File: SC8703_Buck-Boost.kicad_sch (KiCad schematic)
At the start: 0 parts

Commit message: 补充中文版数据手册，原理图放置SC8703芯片
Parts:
- added U1: SC8703, Package_DFN_QFN:QFN-32-1EP_4x4mm_P0.4mm_EP2.65x2.65mm, symbol Zeruns:SC8703
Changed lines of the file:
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@@
 	(generator_version "9.0")
 	(paper "A4")
+	(symbol
+		(lib_id "Zeruns:SC8703")
+		(at 149.86 91.44 0)
+		(unit 1)
+		(exclude_from_sim no)
+		(in_bom yes)
+		(on_board yes)
+		(dnp no)
+		(fields_autoplaced yes)
+		(property "Reference" "U1"
+			(at 149.86 63.5 0)
+			(effects
+				(font
+					(size 1.27 1.27)
+				)
+			)
+		)
+		(property "Value" "SC8703"
+			(at 149.86 66.04 0)
+			(effects
+				(font
+					(size 1.27 1.27)
+				)
+			)
+		)
+		(property "Footprint" "Package_DFN_QFN:QFN-32-1EP_4x4mm_P0.4mm_EP2.65x2.65mm"
+			(at 150.114 121.92 0)
+			(effects
+				(font
+					(size 1.27 1.27)
+				)
+				(hide yes)
+			)
+		)
+		(property "Datasheet" "kicad-embed://SouthChip-Regular_SC8703_datasheet_20241224.pdf"
+			(at 149.86 124.206 0)
+			(effects
+				(font
+					(size 1.27 1.27)
+				)
+				(hide yes)
+			)
+		)
+		(property "Description" "南芯半导体（SouthChip）SC8703 高效率同步 4 管升降压控制器，支持 2.7V~36V 超宽输入输出电压范围，集成 10V/2A 栅极驱动器，可在输入电压高于、低于或等于输出电压时稳定输出，适用于 USB PD、车充、工业设备等场景。"
+			(at 150.368 127 0)
+			(effects
+				(font
+					(size 1.27 1.27)
+				)
+				(hide yes)
+			)
+		)
+		(pin "2"
+		)
+		(pin "1"
+		)
+		(pin "15"
+		)
+		(pin "4"
+		)
+		(pin "31"
+		)
+		(pin "5"
+		)
+		(pin "10"
+		)
+		(pin "33"
+		)
+		(pin "3"
+		)
+		(pin "6"
+		)
+		(pin "7"
+		)
+		(pin "8"
+		)
+		(pin "9"
+		)
+		(pin "12"
+		)
+		(pin "11"
+		)
+		(pin "13"
+		)
+		(pin "14"
+		)
+		(pin "16"
+		)
+		(pin "32"
+		)
+		(pin "30"
+		)
+		(pin "28"
+		)
+		(pin "27"
+		)
+		(pin "26"
+		)
+		(pin "25"
+		)
+		(pin "29"
+		)
+		(pin "22"
+		)
+		(pin "18"
+		)
+		(pin "24"
+		)
+		(pin "20"
+		)
+		(pin "17"
+		)
+		(pin "21"
+		)
+		(pin "23"
+		)
+		(pin "19"
+		)
+		(instances
+			(project ""
+				(path "/00808dcd-76cb-4382-86f8-b718334c603a"
+					(reference "U1")
+					(unit 1)
+				)
+			)
+		)
+	)
 	(sheet_instances
 		(path "/"

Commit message: 原理图完成5%
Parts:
- added C1, C2: 10nF, Capacitor_SMD:C_0402_1005Metric_Pad0.74x0.62mm_HandSolder, symbol Device:C
- added J1: XT30PW-M, Connector_AMASS:AMASS_XT30PW-M_1x02_P2.50mm_Horizontal, symbol Connector:Conn_01x02_Socket
- added J2: Conn_01x02_Socket, Connector_AMASS:AMASS_XT30PW-F_1x02_P2.50mm_Horizontal, symbol Connector:Conn_01x02_Socket
- added Q1, Q2, Q3, Q4: XRS100N06LD, Zeruns:DFN-8_L3.0-W3.0-P0.65-BL-4, symbol Simulation_SPICE:NMOS
- added R1, R3: 12.1k, Resistor_SMD:R_0402_1005Metric_Pad0.72x0.64mm_HandSolder, symbol Device:R
- added R2, R4: 5mR, Resistor_SMD:R_1206_3216Metric_Pad1.30x1.75mm_HandSolder, symbol Device:R
- added RV2: 200k, Potentiometer_THT:Potentiometer_Bourns_3296W_Vertical, symbol Device:R_Potentiometer
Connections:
- net at U1.11 (ILIM1): now also C1.2, R1.2
- net at U1.12 (ILIM2): now also C2.2, R3.2
- new net: Q1.3 (S), Q2.1 (D)
- new net: Q1.1 (D), R2.2
- new net: J1.2 (Pin_2), R2.1
- new net: R3.1, RV2.1, RV2.2
- new net: Q3.1 (D), R4.1
- new net: Q3.3 (S), Q4.1 (D)
- new net GND: C1.1, C2.1, R1.1, RV2.3
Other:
- moved on the sheet: U1

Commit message: 原理图完成80%，上传数据手册
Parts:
- added C10, C11, C5, C6, C7, C9: 10uF, Capacitor_SMD:C_1206_3216Metric_Pad1.33x1.80mm_HandSolder, symbol Device:C
- added C12, C17, C18, C8: 100nF, Capacitor_SMD:C_0402_1005Metric_Pad0.74x0.62mm_HandSolder, symbol Device:C
- added C13: 15nF, Capacitor_SMD:C_0402_1005Metric_Pad0.74x0.62mm_HandSolder, symbol Device:C
- added C14, C15: 47pF, Capacitor_SMD:C_0402_1005Metric_Pad0.74x0.62mm_HandSolder, symbol Device:C
- added C16, C19, C20: 1uF, Capacitor_SMD:C_0402_1005Metric_Pad0.74x0.62mm_HandSolder, symbol Device:C
- added C21, C22: NC, Capacitor_SMD:C_0603_1608Metric_Pad1.08x0.95mm_HandSolder, symbol Device:C
- added C3: 220uF, Capacitor_SMD:CP_Elec_10x10.5, symbol Device:C_Polarized_US
- added C4: 330uF, Capacitor_SMD:CP_Elec_10x10.5, symbol Device:C_Polarized_US
- added D1, D2: TPB2A100-123FL, Diode_SMD:D_SOD-123F, symbol Device:D_Schottky
- added J3: USB_C_Receptacle_USB2.0_16P, Connector_USB:USB_C_Receptacle_HCTL_HC-TYPE-C-16P-01A, symbol Connector:USB_C_Receptacle_USB2.0_16P
- added L1: 4.7uH, Inductor_SMD:L_APV_APH1265, symbol Device:L
- added R10, R11, R12, R9: 510R, Resistor_SMD:R_0402_1005Metric_Pad0.72x0.64mm_HandSolder, symbol Device:R
- added R13, R14, R15, R16: 0R, Resistor_SMD:R_0603_1608Metric_Pad0.98x0.95mm_HandSolder, symbol Device:R
- added R17, R18: NC, Resistor_SMD:R_0603_1608Metric_Pad0.98x0.95mm_HandSolder, symbol Device:R
- added R5: NC, Resistor_SMD:R_0402_1005Metric_Pad0.72x0.64mm_HandSolder, symbol Device:R
- added R6: 68k, Resistor_SMD:R_0402_1005Metric_Pad0.72x0.64mm_HandSolder, symbol Device:R
- added R7: 15k, Resistor_SMD:R_0402_1005Metric_Pad0.72x0.64mm_HandSolder, symbol Device:R
- added R8: 1.74k, Resistor_SMD:R_0402_1005Metric_Pad0.72x0.64mm_HandSolder, symbol Device:R
- added RV1: 50k, Potentiometer_THT:Potentiometer_Bourns_3296X_Horizontal, symbol Device:R_Potentiometer
- added U2: CH224Q, Zeruns:DFN-10_L2.0-W2.0-P0.40-BL-EP, symbol Zeruns:CH224Q
- J2: value Conn_01x02_Socket -> XT30PW-F
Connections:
- net GND: now also J1.1 (Pin_1), J2.1 (Pin_1), Q2.3 (S), Q4.3 (S), U1.1 (CE#), U1.14 (AGND), U1.2 (AGND), U1.25 (PGND), U1.33 (PGND), U1.9 (AGND), C10.2, C11.2, C12.1, C13.1, C16.2, C19.2, C20.2, C21.1, C22.1, C3.2, C4.2, C5.2, C6.2, C7.2, C8.1, C9.2, R5.1, R6.1, R8.1
- net SW1: now reaches Q1.3 (S), Q2.1 (D)
- net SW1: now also U1.27 (SW1), C17.2, L1.1, R17.2
- net at Q2.2 (G): now also R14.2
- net ILIM1: now reaches C1.2, R1.2, U1.11 (ILIM1)
- net at Q1.1 (D), R2.2: now also R10.1
- net at Q1.2 (G): now also R13.2
- net VOUT: now reaches J2.2 (Pin_2)
- net VOUT: now also R4.2, U1.19 (VOUT), C10.1, C11.1, C12.2, C20.1, C4.1, C9.1, R12.1, RV1.3
- net VIN: now reaches J1.2 (Pin_2), R2.1
- net VIN: now also U1.30 (VIN), U1.7 (UVLO), C16.1, C3.1, C5.1, C6.1, C7.1, C8.2, R9.1
- net ILIM2: now reaches C2.2, R3.2, U1.12 (ILIM2)
- net at Q3.1 (D), R4.1: now also R11.1
- net at Q3.2 (G): now also R15.1
- net SW2: now reaches Q3.3 (S), Q4.1 (D)
- net SW2: now also U1.22 (SW2), C18.2, L1.2, R18.2
- net FREQ: now reaches U1.10 (FREQ)
- net FREQ: now also R5.2
- net at U1.15 (COMP): now also R7.2
- net FB: now reaches U1.16 (FB)
- net FB: now also R8.2, RV1.1, RV1.2
- net SNS2_N: now reaches U1.17 (SNS2N)
- net SNS2_N: now also C15.2, R12.2
- net SNS2_P: now reaches U1.18 (SNS2P)
- net SNS2_P: now also C15.1, R11.2
- net BT2: now reaches U1.20 (BT2)
- net BT2: now also C18.1, D2.1 (K)
- net HD2: now reaches U1.21 (HD2)
- net HD2: now also R15.2
- net LD2: now reaches U1.23 (LD2)
- net LD2: now also R16.2
- net VCC: now reaches U1.24 (VCC)
- net VCC: now also C19.1, D1.2 (A), D2.2 (A)
- net LD1: now reaches U1.26 (LD1)
- net LD1: now also R14.1
- net HD1: now reaches U1.28 (HD1)
- net HD1: now also R13.1
- net BT1: now reaches U1.29 (BT1)
- net BT1: now also C17.1, D1.1 (K)
- net SNS1_N: now reaches U1.31 (SNS1N)
- net SNS1_N: now also C14.2, R10.2
- net SNS1_P: now reaches U1.32 (SNS1P)
- net SNS1_P: now also C14.1, R9.2
- net at U1.8 (DT): now also R6.2
- net at Q4.2 (G): now also R16.1
- new net: C22.2, R18.1
- new net: C21.2, R17.1
- new net: C13.2, R7.1
- new net: J3.A1 (GND), J3.A12 (GND), J3.B1 (GND), J3.B12 (GND)
- new net: J3.A4 (VBUS), J3.A9 (VBUS), J3.B4 (VBUS), J3.B9 (VBUS)
- no-connect marks 0 -> 5
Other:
- moved on the sheet: C1, C2, J1, J2, Q1, Q2, Q3, Q4, R1, R2, R3, R4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

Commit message: 完成原理图设计
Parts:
- added C23: 1uF, Capacitor_SMD:C_0402_1005Metric_Pad0.74x0.62mm_HandSolder, symbol Device:C
- added D1: LED-RED, LED_SMD:LED_0603_1608Metric_Pad1.05x0.95mm_HandSolder, symbol Device:LED
- added D4: SB1045L, kicad_api_lib:SB1045L, symbol SB1045L:SB1045L
- added R11, R12: 12.1k, Resistor_SMD:R_0402_1005Metric_Pad0.72x0.64mm_HandSolder, symbol Device:R
- added R21: 210k, Resistor_SMD:R_0402_1005Metric_Pad0.72x0.64mm_HandSolder, symbol Device:R
- renumbered C21 to C1, C4 to C10, C9 to C11, C10 to C12, C11 to C13, C12 to C14, C16 to C15, C17 to C16, C19 to C17, C1 to C19, C22 to C2, C2 to C21, C13 to C22, C14 to C3, C15 to C4, C3 to C5, C5 to C6, C6 to C7, C7 to C8, C8 to C9, D1 to D2, D2 to D3, Q3 to Q2, Q2 to Q3, R17 to R1, R15 to R10, R14 to R13, R16 to R14, R6 to R15, R5 to R16, R1 to R17, R3 to R18, R7 to R19, R18 to R2, R8 to R20, R9 to R3, R10 to R4, R11 to R5, R12 to R6, R2 to R7, R4 to R8, R13 to R9, RV2 to RV1, RV1 to RV2
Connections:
- net GND: now also J3.A1 (GND), J3.A12 (GND), J3.B1 (GND), J3.B12 (GND), J3.S1 (SHIELD), U2.11 (EP), C23.1, D1.1 (K), R21.2
- net VIN: now also D4.2 (K)
- net VOUT: now also R11.2, R12.2
- net VBUS: now reaches U2.1 (VHV)
- net VBUS: now also J3.A4 (VBUS), J3.A9 (VBUS), J3.B4 (VBUS), J3.B9 (VBUS), U2.8 (VBUS), C23.2, D4.1 (A), D4.3 (A)
- net D+: now reaches U2.4 (DP)
- net D+: now also J3.A6 (D+), J3.B6 (D+)
- net D-: now reaches U2.5 (DM)
- net D-: now also J3.A7 (D-), J3.B7 (D-)
- net CC2: now reaches U2.6 (CC2)
- net CC2: now also J3.B5 (CC2)
- net CC1: now reaches U2.7 (CC1)
- net CC1: now also J3.A5 (CC1)
- net at U2.9 (CFG1): now also R21.1
- new net: D1.2 (A), R11.1, R12.1
- no-connect marks 5 -> 10
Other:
- moved on the sheet: C1, C15, C16, C17, C18, C19, C2, C20, C21, C22, D2, D3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

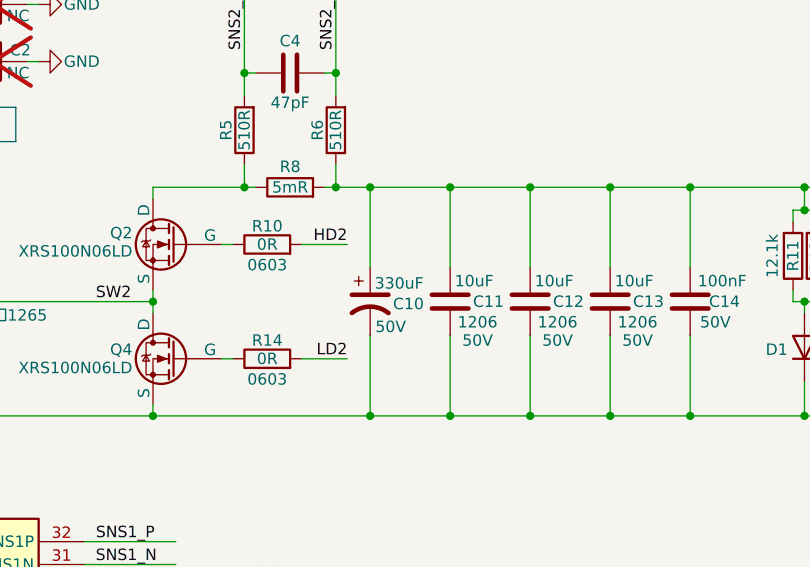
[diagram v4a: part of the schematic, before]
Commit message: 修正输出电容数值
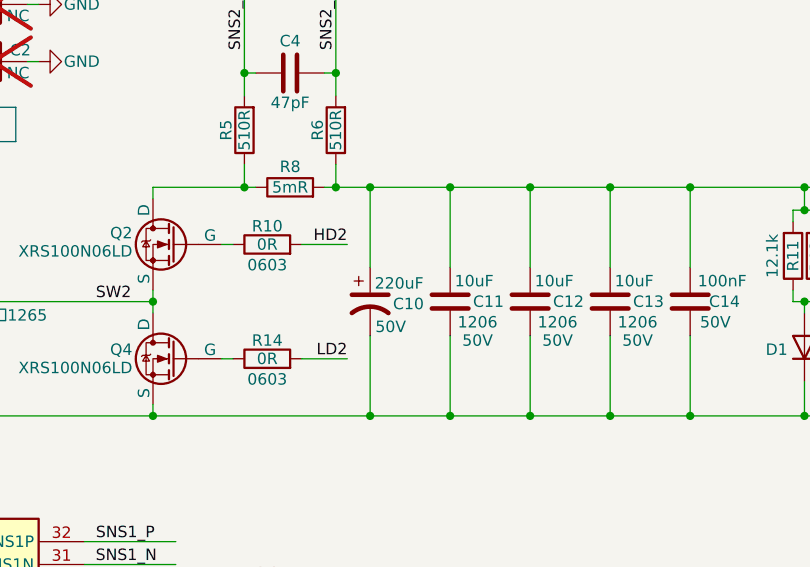
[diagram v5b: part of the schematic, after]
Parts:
- C10: value 330uF -> 220uF
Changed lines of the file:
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@@
 			)
 		)
-		(property "Value" "330uF"
+		(property "Value" "220uF"
 			(at 192.278 50.038 0)
 			(effects

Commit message: PCB完成95%
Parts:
- added C24, C25: 220uF, Capacitor_SMD:CP_Elec_10x10.5, symbol Device:C_Polarized_US
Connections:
- net GND: now also C24.2, C25.2
- net VIN: now also C24.1
- net VOUT: now also C25.1
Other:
- moved on the sheet: C11, C12, C13, C14, C5, D1, J1, J2, R11, R12

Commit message: 设计完成，下单打样
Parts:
- RV1: footprint Potentiometer_THT:Potentiometer_Bourns_3296W_Vertical -> Potentiometer_THT:Potentiometer_Bourns_3296X_Horizontal
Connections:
- net GND: now also RV1.1; no longer RV1.3
- net at R18.1, RV1.2: now also RV1.3; no longer RV1.1
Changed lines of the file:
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@@
 		)
 	)
+	(text_box "输出电压：2.5V-36.2V  可调"
+		(exclude_from_sim no)
+		(at 88.9 144.78 0)
+		(size 30.48 3.81)
+		(margins 0.9525 0.9525 0.9525 0.9525)
+		(stroke
+			(width 0)
+			(type solid)
+		)
+		(fill
+			(type none)
+		)
+		(effects
+			(font
+				(face "HarmonyOS Sans SC")
+				(size 1.524 1.524)
+			)
+			(justify left)
+		)
+	)
 	(junction
 		(at 68.58 64.77)
@@
 	)
 	(symbol
+		(lib_id "Device:R_Potentiometer")
+		(at 90.17 115.57 90)
+		(mirror x)
+		(unit 1)
+		(exclude_from_sim no)
+		(in_bom yes)
+		(on_board yes)
+		(dnp no)
+		(property "Reference" "RV1"
+			(at 90.17 113.284 90)
+			(effects
+				(font
+					(size 1.27 1.27)
+				)
+			)
+		)
+		(property "Value" "200k"
+			(at 90.17 115.57 90)
+			(effects
+				(font
+					(size 1.27 1.27)
+				)
+			)
+		)
+		(property "Footprint" "Potentiometer_THT:Potentiometer_Bourns_3296X_Horizontal"
+			(at 90.17 115.57 0)
+			(effects
+				(font
+					(size 1.27 1.27)
+				)
+				(hide yes)
+			)
+		)
+		(property "Datasheet" "~"
+			(at 90.17 115.57 0)
+			(effects
+				(font
+					(size 1.27 1.27)
+				)
+				(hide yes)
+			)
+		)
+		(property "Description" "Potentiometer"
+			(at 90.17 115.57 0)
+			(effects
+				(font
+					(size 1.27 1.27)
+				)
+				(hide yes)
+			)
+		)
+		(pin "3"
+		)
+		(pin "2"
+		)
+		(pin "1"
+		)
+		(instances
+			(project "SC8703_Buck-Boost"
+				(path "/00808dcd-76cb-4382-86f8-b718334c603a"
+					(reference "RV1")
+					(unit 1)
+				)
+			)
+		)
+	)
+	(symbol
 		(lib_id "Device:R")
 		(at 100.33 96.52 90)
@@
 					(unit 1)
 				)
-			)
-		)
-	)
-	(symbol
-		(lib_id "Device:R_Potentiometer")
-		(at 90.17 115.57 270)
-		(unit 1)
-		(exclude_from_sim no)
-		(in_bom yes)
-		(on_board yes)
-		(dnp no)
-		(property "Reference" "RV1"
-			(at 90.17 113.284 90)
-			(effects
-				(font
-					(size 1.27 1.27)
-				)
-			)
-		)
-		(property "Value" "200k"
-			(at 90.17 115.57 90)
-			(effects
-				(font
-					(size 1.27 1.27)
-				)
-			)
-		)
-		(property "Footprint" "Potentiometer_THT:Potentiometer_Bourns_3296W_Vertical"
-			(at 90.17 115.57 0)
-			(effects
-				(font
-					(size 1.27 1.27)
-				)
-				(hide yes)
-			)
-		)
-		(property "Datasheet" "~"
-			(at 90.17 115.57 0)
-			(effects
-				(font
-					(size 1.27 1.27)
-				)
-				(hide yes)
-			)
-		)
-		(property "Description" "Potentiometer"
-			(at 90.17 115.57 0)
-			(effects
-				(font
-					(size 1.27 1.27)
-				)
-				(hide yes)
-			)
-		)
-		(pin "3"
-		)
-		(pin "2"
-		)
-		(pin "1"
-		)
-		(instances
-			(project "SC8703_Buck-Boost"
-				(path "/00808dcd-76cb-4382-86f8-b718334c603a"
-					(reference "RV1")
-					(unit 1)
-				)

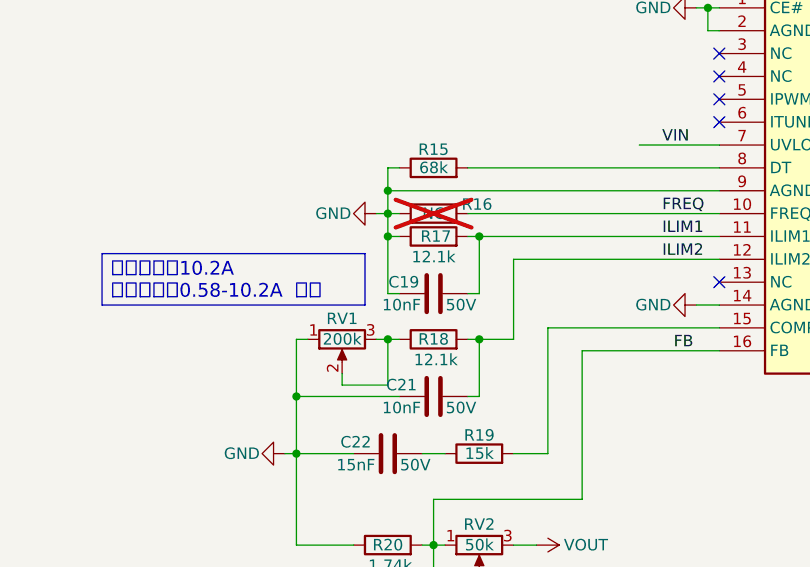
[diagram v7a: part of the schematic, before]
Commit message: 导出原理图和丝印图PDF
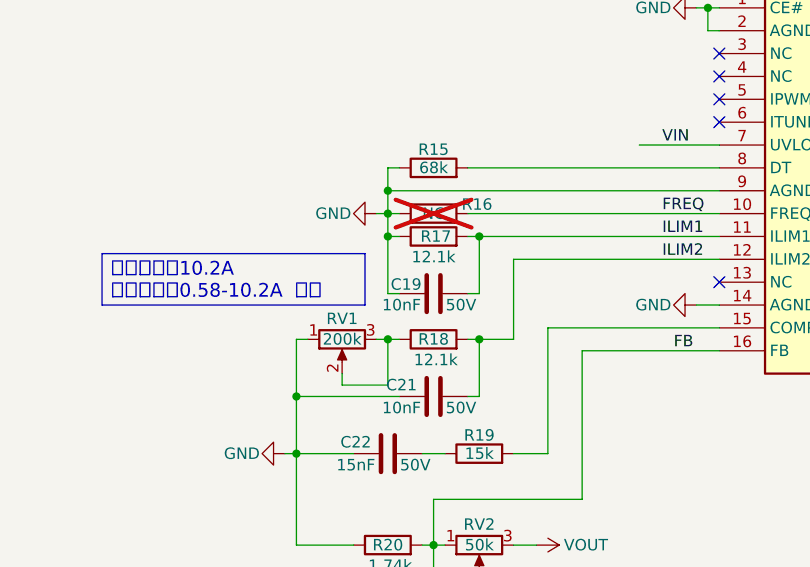
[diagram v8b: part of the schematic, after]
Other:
- company: (none) -> Zeruns    blog.zeruns.com
- title: (none) -> 基于SC8703的Buck-Boost升降压DCDC电源
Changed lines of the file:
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@@
 	(generator_version "9.0")
 	(paper "A4")
+	(title_block
+		(title "基于SC8703的Buck-Boost升降压DCDC电源")
+		(company "Zeruns    blog.zeruns.com")
+	)
 	(text_box "RC吸收电路"
 		(exclude_from_sim no)
@@
 	)
 	(image
-		(at 74.93 101.6)
-		(scale 0.440304)
+		(at 67.31 99.06)
+		(scale 0.814833)
 		(data "iVBORw0KGgoAAAANSUhEUgAAAjAAAACfCAIAAABoRnQqAAAAA3NCSVQICAjb4U/gAAAgAElEQVR4"
 			"nO3dZ0ATSRsA4DebAoTeO0hVqogCgoigYtezd0WxH/Z6KPaC2MvZG6Ji72Lvng0LCNIU6VKlQwhJ"
@@
 	)
 	(image
-		(at 74.93 95.25)
-		(scale 0.429533)
+		(at 67.31 86.36)
+		(scale 0.826843)
 		(data "iVBORw0KGgoAAAANSUhEUgAAAjUAAADACAIAAABztwVMAAAAA3NCSVQICAjb4U/gAAAgAElEQVR4"
 			"nO3dZ0ATSRsH8IdNIZTQe5UuqIgoCIoIKnbsnVexnBWwe56K/bCX0zs9e0Oxt1Oxnr1iAbEgRalS"
@@
 		(dnp no)
 		(property "Reference" "C19"
-			(at 97.028 109.22 90)
+			(at 97.282 109.474 90)
 			(effects
 				(font
